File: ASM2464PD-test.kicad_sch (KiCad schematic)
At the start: 1 part

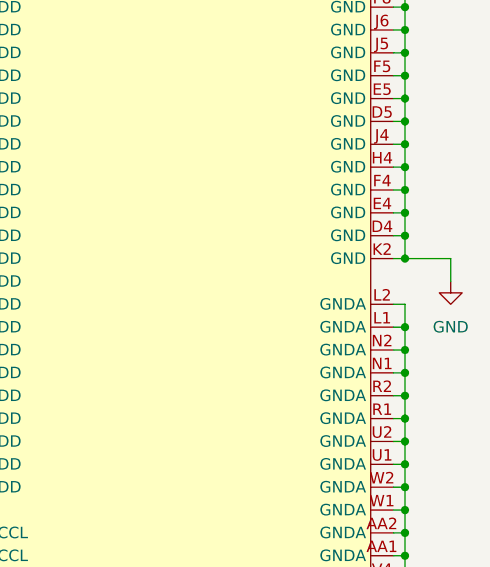
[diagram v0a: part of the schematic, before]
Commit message: Connected the 2 grounds
what's the difference anyway
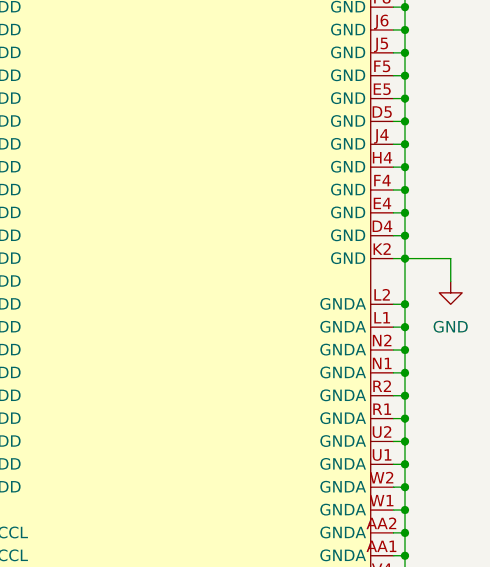
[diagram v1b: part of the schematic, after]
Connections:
- net GNDA is gone; now on net GND: U1.AA1 (GNDA), U1.AA12 (GNDA), U1.AA14 (GNDA), U1.AA16 (GNDA), U1.AA18 (GNDA), U1.AA2 (GNDA), U1.AA20 (GNDA), U1.AA21 (GNDA), U1.AA5 (GNDA), U1.AA9 (GNDA), U1.L1 (GNDA), U1.L2 (GNDA), U1.L4 (GNDA), U1.L5 (GNDA), U1.M20 (GNDA), U1.M21 (GNDA), U1.N1 (GNDA), U1.N17 (GNDA), U1.N18 (GNDA), U1.N2 (GNDA), U1.N4 (GNDA), U1.N5 (GNDA), U1.P17 (GNDA), U1.P18 (GNDA), U1.P20 (GNDA), U1.P21 (GNDA), U1.P4 (GNDA), U1.P5 (GNDA), U1.R1 (GNDA), U1.R2 (GNDA), U1.T17 (GNDA), U1.T18 (GNDA), U1.T20 (GNDA), U1.T21 (GNDA), U1.T4 (GNDA), U1.T5 (GNDA), U1.U1 (GNDA), U1.U17 (GNDA), U1.U18 (GNDA), U1.U2 (GNDA), U1.U4 (GNDA), U1.U5 (GNDA), U1.V11 (GNDA), U1.V13 (GNDA), U1.V14 (GNDA), U1.V16 (GNDA), U1.V17 (GNDA), U1.V18 (GNDA), U1.V20 (GNDA), U1.V21 (GNDA), U1.V4 (GNDA), U1.V5 (GNDA), U1.V6 (GNDA), U1.V8 (GNDA), U1.V9 (GNDA), U1.W1 (GNDA), U1.W2 (GNDA), U1.Y12 (GNDA), U1.Y14 (GNDA), U1.Y16 (GNDA), U1.Y18 (GNDA), U1.Y20 (GNDA), U1.Y21 (GNDA), U1.Y3 (GNDA), U1.Y5 (GNDA), U1.Y9 (GNDA)
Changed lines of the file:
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@@
   (junction (at 270.51 185.42) (diameter 0) (color 0 0 0 0)
   )
+  (junction (at 270.51 114.3) (diameter 0) (color 0 0 0 0)
+  )
   (junction (at 220.98 119.38) (diameter 0) (color 0 0 0 0)
   )
@@
     (stroke (width 0) (type default))
   )
+  (wire (pts (xy 270.51 109.22) (xy 270.51 114.3))
+    (stroke (width 0) (type default))
+  )

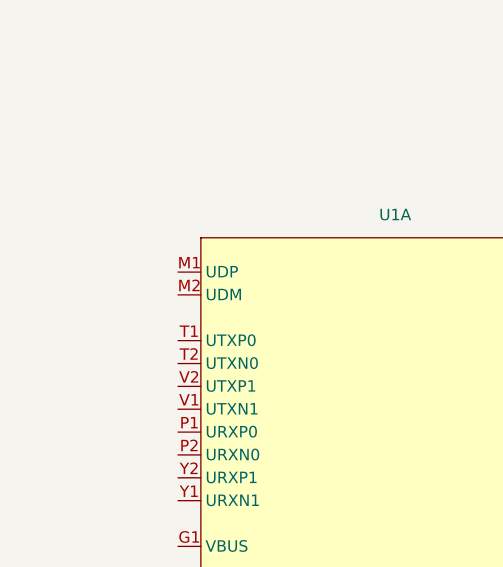
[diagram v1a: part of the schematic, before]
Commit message: Added some keywords to readme
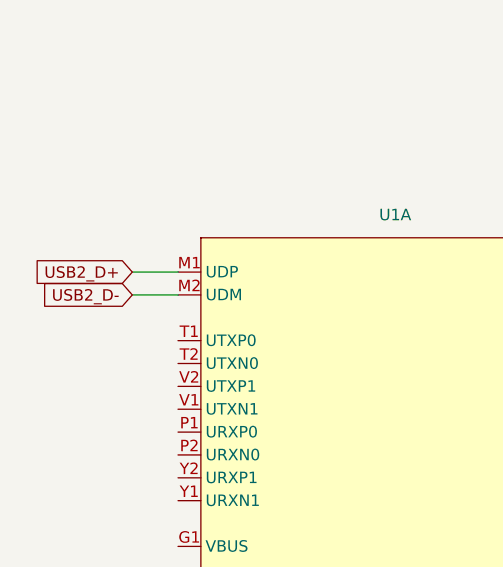
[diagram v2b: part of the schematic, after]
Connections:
- net USB2_D+: now reaches U1.M1 (UDP)
- net USB2_D-: now reaches U1.M2 (UDM)
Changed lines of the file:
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@@
+    (stroke (width 0) (type default))
+  )
+  (wire (pts (xy 59.69 93.98) (xy 64.77 93.98))
     (stroke (width 0) (type default))
   )
@@
     (stroke (width 0) (type default))
   )
+  (wire (pts (xy 59.69 96.52) (xy 64.77 96.52))
+    (stroke (width 0) (type default))
+  )
   (wire (pts (xy 269.24 213.36) (xy 270.51 213.36))
     (stroke (width 0) (type default))
@@
   (wire (pts (xy 269.24 223.52) (xy 270.51 223.52))
     (stroke (width 0) (type default))
+  )
+  (global_label "USB2_D-" (shape input) (at 59.69 96.52 180) (fields_autoplaced)
+    (effects (font (size 1.27 1.27)) (justify right))
+    (property "Intersheetrefs" "${INTERSHEET_REFS}" (at 47.8753 96.52 0)
+      (effects (font (size 1.27 1.27)) (justify right) hide)
+    )
+  )
+  (global_label "USB2_D+" (shape input) (at 59.69 93.98 180) (fields_autoplaced)
+    (effects (font (size 1.27 1.27)) (justify right))
+    (property "Intersheetrefs" "${INTERSHEET_REFS}" (at 47.8753 93.98 0)
+      (effects (font (size 1.27 1.27)) (justify right) hide)
+    )
   )
   (symbol (lib_id "power:GND") (at 275.59 111.76 0) (unit 1)
@@
   )
   (symbol (lib_id "A_my_stuff:ASM2464PD") (at 87.63 195.58 0) (unit 1)
-    (in_bom yes) (on_board yes) (dnp no) (fields_autoplaced)
+    (in_bom yes) (on_board yes) (dnp no)
     (property "Reference" "U1" (at 88.9 87.63 0)
       (effects (font (size 1.27 1.27)))

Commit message: Added ports and definitely didn't clone reddit board lol
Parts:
- added C1, C10, C11, C12, C13, C14, C15, C16, C2, C3, C4, C5, C6, C7, C8, C9: 0.22u, Capacitor_SMD:C_0402_1005Metric, symbol Device:C_Small
- added J1: USB_C_Receptacle, Connector_USB:USB_C_Receptacle_Amphenol_12401610E4-2A, symbol Connector:USB_C_Receptacle
- added J2: Bus_M.2_Socket_M, A_my_stuff:m-key, symbol Connector:Bus_M.2_Socket_M
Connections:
- net GND: now also J1.A1 (GND), J1.A12 (GND), J1.B1 (GND), J1.B12 (GND), J1.S1 (SHIELD), J2.1 (GND), J2.15 (GND), J2.21 (GND), J2.27 (GND), J2.3 (GND), J2.33 (GND), J2.39 (GND), J2.45 (GND), J2.51 (GND), J2.57 (GND), J2.71 (GND), J2.73 (GND), J2.75 (GND), J2.9 (GND)
- net USB2_D+: now also J1.A6 (D+), J1.B6 (D+)
- net USB2_D-: now also J1.A7 (D-), J1.B7 (D-)
- net PCIe_RX3+: now reaches U1.AA13 (PRXP3)
- net PCIe_RX3+: now also J2.7 (PERp3)
- net PCIe_TX3-: now reaches U1.AA15 (PTXN3)
- net PCIe_TX3-: now also C8.1
- net PCIe_TX2-: now reaches U1.AA17 (PTXN2)
- net PCIe_TX2-: now also C6.1
- net PCIe_RX2-: now reaches U1.AA19 (PRXN2)
- net PCIe_RX2-: now also J2.17 (PERn2)
- net CC1: now reaches U1.AA6 (CC1)
- net CC1: now also J1.A5 (CC1)
- net REFCLK+: now reaches U1.AA8 (REFCLKP0)
- net REFCLK+: now also J2.55 (REFCLKp)
- net PERST#: now reaches U1.G21 (PERST0#)
- net PERST#: now also J2.50 (~{PERST})
- net SBU2: now reaches U1.J1 (SBU2)
- net SBU2: now also J1.B8 (SBU2)
- net SBU1: now reaches U1.K1 (SBU1)
- net SBU1: now also J1.A8 (SBU1)
- net PCIe_RX0-: now reaches U1.N20 (PRXN0)
- net PCIe_RX0-: now also J2.41 (PERn0/SATA-B+)
- net PCIe_RX0+: now reaches U1.N21 (PRXP0)
- net PCIe_RX0+: now also J2.43 (PERp0/SATA-B-)
- net URX0+: now reaches U1.P1 (URXP0)
- net URX0+: now also C10.2
- net URX0-: now reaches U1.P2 (URXN0)
- net URX0-: now also C9.2
- net PCIe_TX0+: now reaches U1.R20 (PTXP0)
- net PCIe_TX0+: now also C1.1
- net PCIe_TX0-: now reaches U1.R21 (PTXN0)
- net PCIe_TX0-: now also C2.1
- net UTX0+: now reaches U1.T1 (UTXP0)
- net UTX0+: now also C12.2
- net UTX0-: now reaches U1.T2 (UTXN0)
- net UTX0-: now also C11.2
- net PCIe_TX1+: now reaches U1.U20 (PTXP1)
- net PCIe_TX1+: now also C3.1
- net PCIe_TX1-: now reaches U1.U21 (PTXN1)
- net PCIe_TX1-: now also C4.1
- net UTX1-: now reaches U1.V1 (UTXN1)
- net UTX1-: now also C15.2
- net UTX1+: now reaches U1.V2 (UTXP1)
- net UTX1+: now also C16.2
- net PCIe_RX1-: now reaches U1.W20 (PRXN1)
- net PCIe_RX1-: now also J2.29 (PERn1)
- net PCIe_RX1+: now reaches U1.W21 (PRXP1)
- net PCIe_RX1+: now also J2.31 (PERp1)
- net URX1-: now reaches U1.Y1 (URXN1)
- net URX1-: now also C13.2
- net PCIe_RX3-: now reaches U1.Y13 (PRXN3)
- net PCIe_RX3-: now also J2.5 (PERn3)
- net PCIe_TX3+: now reaches U1.Y15 (PTXP3)
- net PCIe_TX3+: now also C7.1
- net PCIe_TX2+: now reaches U1.Y17 (PTXP2)
- net PCIe_TX2+: now also C5.1
- net PCIe_RX2+: now reaches U1.Y19 (PRXP2)
- net PCIe_RX2+: now also J2.19 (PERp2)
- net URX1+: now reaches U1.Y2 (URXP1)
- net URX1+: now also C14.2
- net CC2: now reaches U1.Y6 (CC2)
- net CC2: now also J1.B5 (CC2)
- net REFCLK-: now reaches U1.Y8 (REFCLKN0)
- net REFCLK-: now also J2.53 (REFCLKn)
- new net: J1.A4 (VBUS), J1.A9 (VBUS), J1.B4 (VBUS), J1.B9 (VBUS)
- new net: J2.12 (3.3V), J2.14 (3.3V), J2.16 (3.3V), J2.18 (3.3V), J2.2 (3.3V), J2.4 (3.3V), J2.70 (3.3V), J2.72 (3.3V), J2.74 (3.3V)
- new net PCIe_TX0_C+: C1.2, J2.49 (PETp0/SATA-A+)
- new net PCIe_TX0_C-: C2.2, J2.47 (PETn0/SATA-A-)
- new net PCIe_TX1_C+: C3.2, J2.37 (PETp1)
- new net PCIe_TX1_C-: C4.2, J2.35 (PETn1)
- new net PCIe_TX2_C+: C5.2, J2.25 (PETp2)
- new net PCIe_TX2_C-: C6.2, J2.23 (PETn2)
- new net PCIe_TX3_C+: C7.2, J2.13 (PETp3)
- new net PCIe_TX3_C-: C8.2, J2.11 (PETn3)
- new net URX0_C+: C10.1, J1.B11 (RX1+)
- new net URX0_C-: C9.1, J1.B10 (RX1-)
- new net URX1_C+: C14.1, J1.A11 (RX2+)
- new net URX1_C-: C13.1, J1.A10 (RX2-)
- new net UTX0_C+: C12.1, J1.A2 (TX1+)
- new net UTX0_C-: C11.1, J1.A3 (TX1-)
- new net UTX1_C+: C16.1, J1.B2 (TX2+)
- new net UTX1_C-: C15.1, J1.B3 (TX2-)
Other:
- note added: "idk if these caps are the right value. these signals probably need some more protection and stuff on them too."
- moved on the sheet: U1A, U1B, U1C

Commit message: Tried adding power fills under the chip
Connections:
- net VCCH: now reaches U1.D13 (VCCH), U1.D6 (VCCH), U1.D8 (VCCH), U1.D9 (VCCH), U1.E13 (VCCH), U1.E6 (VCCH), U1.E8 (VCCH), U1.E9 (VCCH), U1.F13 (VCCH), U1.F6 (VCCH), U1.H6 (VCCH)
- net VDD: now reaches U1.D14 (VDD), U1.D16 (VDD), U1.E11 (VDD), U1.E14 (VDD), U1.E16 (VDD), U1.F11 (VDD), U1.F14 (VDD), U1.F16 (VDD), U1.F9 (VDD), U1.H11 (VDD), U1.H13 (VDD), U1.H14 (VDD), U1.H16 (VDD), U1.H9 (VDD), U1.J13 (VDD), U1.J14 (VDD), U1.J16 (VDD), U1.J17 (VDD), U1.J18 (VDD), U1.J20 (VDD), U1.J21 (VDD), U1.J8 (VDD), U1.J9 (VDD), U1.K20 (VDD), U1.K21 (VDD), U1.L11 (VDD), U1.L14 (VDD), U1.L8 (VDD), U1.N14 (VDD), U1.N8 (VDD), U1.P13 (VDD), U1.P14 (VDD), U1.P8 (VDD), U1.T11 (VDD), U1.T13 (VDD), U1.T14 (VDD), U1.T8 (VDD), U1.T9 (VDD), U1.U8 (VDD), U1.U9 (VDD)
- net VCCL: now reaches U1.L16 (VCCL), U1.L17 (VCCL), U1.L18 (VCCL), U1.L20 (VCCL), U1.L21 (VCCL), U1.L6 (VCCL), U1.N16 (VCCL), U1.N6 (VCCL), U1.P16 (VCCL), U1.P6 (VCCL), U1.T16 (VCCL), U1.T6 (VCCL), U1.U11 (VCCL), U1.U13 (VCCL), U1.U14 (VCCL), U1.U16 (VCCL), U1.U6 (VCCL)
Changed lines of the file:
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@@
   (junction (at 398.78 228.6) (diameter 0) (color 0 0 0 0)
   )
+  (junction (at 349.25 20.32) (diameter 0) (color 0 0 0 0)
+  )
   (junction (at 349.25 76.2) (diameter 0) (color 0 0 0 0)
   )
@@
   (junction (at 349.25 137.16) (diameter 0) (color 0 0 0 0)
   )
+  (junction (at 349.25 124.46) (diameter 0) (color 0 0 0 0)
+  )
   (junction (at 398.78 152.4) (diameter 0) (color 0 0 0 0)
   )
@@
   (junction (at 349.25 134.62) (diameter 0) (color 0 0 0 0)
   )
+  (junction (at 349.25 170.18) (diameter 0) (color 0 0 0 0)
+  )
   (junction (at 398.78 111.76) (diameter 0) (color 0 0 0 0)
   )
@@
     (stroke (width 0) (type default))
   )
+  (wire (pts (xy 345.44 19.05) (xy 345.44 20.32))
+    (stroke (width 0) (type default))
+  )
   (wire (pts (xy 397.51 220.98) (xy 398.78 220.98))
     (stroke (width 0) (type default))
@@
     (stroke (width 0) (type default))
   )
+  (wire (pts (xy 346.71 170.18) (xy 349.25 170.18))
+    (stroke (width 0) (type default))
+  )
   (wire (pts (xy 397.51 180.34) (xy 398.78 180.34))
     (stroke (width 0) (type default))
@@
     (stroke (width 0) (type default))
   )
+  (wire (pts (xy 346.71 124.46) (xy 349.25 124.46))
+    (stroke (width 0) (type default))
+  )
   (wire (pts (xy 349.25 175.26) (xy 349.25 177.8))
     (stroke (width 0) (type default))
@@
   )
   (wire (pts (xy 55.88 119.38) (xy 63.5 119.38))
+    (stroke (width 0) (type default))
+  )
+  (wire (pts (xy 345.44 20.32) (xy 349.25 20.32))
     (stroke (width 0) (type default))
   )
@@
     )
   )
+  (global_label "VCCH" (shape input) (at 346.71 170.18 180) (fields_autoplaced)
+    (effects (font (size 1.27 1.27)) (justify right))
+    (property "Intersheetrefs" "${INTERSHEET_REFS}" (at 338.7657 170.18 0)
+      (effects (font (size 1.27 1.27)) (justify right) hide)
+    )
+  )
   (global_label "PCIe_TX0+" (shape input) (at 265.43 128.27 180) (fields_autoplaced)
     (effects (font (size 1.27 1.27)) (justify right))
@@
     (effects (font (size 1.27 1.27)) (justify right))
     (property "Intersheetrefs" "${INTERSHEET_REFS}" (at 253.7967 115.57 0)
+      (effects (font (size 1.27 1.27)) (justify right) hide)
+    )
+  )
+  (global_label "VCCL" (shape input) (at 346.71 124.46 180) (fields_autoplaced)
+    (effects (font (size 1.27 1.27)) (justify right))
+    (property "Intersheetrefs" "${INTERSHEET_REFS}" (at 339.0681 124.46 0)
       (effects (font (size 1.27 1.27)) (justify right) hide)
     )
@@
         )
       )
+    )
+  )
+  (symbol (lib_id "power:VDD") (at 345.44 19.05 0) (unit 1)
+    (in_bom yes) (on_board yes) (dnp no) (fields_autoplaced)
+    (property "Reference" "#PWR05" (at 345.44 22.86 0)
+      (effects (font (size 1.27 1.27)) hide)
+    )
+    (property "Value" "VDD" (at 345.44 13.97 0)
+      (effects (font (size 1.27 1.27)))
+    )
+    (property "Footprint" "" (at 345.44 19.05 0)
+      (effects (font (size 1.27 1.27)) hide)
+    )
+    (property "Datasheet" "" (at 345.44 19.05 0)
+      (effects (font (size 1.27 1.27)) hide)
+    )
+    (pin "1")
+    (instances
+      (project "ASM2464PD-test"
+        (path "/b2a945ac-f788-482b-9831-47d865c602eb"
+          (reference "#PWR05") (unit 1)
+        )
+      )

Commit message: forgor some power pins
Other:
- company: (none) -> WifiCable
- title: (none) -> ASM2464PD-test
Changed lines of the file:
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@@
 (kicad_sch (version 20230121) (generator eeschema)
   (paper "A3")
+  (title_block
+    (title "ASM2464PD-test")
+    (company "WifiCable")
+  )
   (junction (at 398.78 114.3) (diameter 0) (color 0 0 0 0)
   )

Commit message: Labeled power rails, upgraded to KiCad 8
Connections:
- net 3.3VA: now reaches U1.H5 (VCCA33)
- net VCCH renamed 3.3V
- net VCCL renamed 1.8V
- net VDD renamed 1.05V

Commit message: Updated symbol to match reference schematic
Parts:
- added unit 4 of U1
- added unit 5 of U1
- added unit 6 of U1
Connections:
- net 1.8V: now also U1.L16 (VCCL), U1.L17 (VCCL), U1.L18 (VCCL), U1.L20 (VCCL), U1.L21 (VCCL), U1.L6 (VCCL), U1.N16 (VCCL), U1.N6 (VCCL), U1.P16 (VCCL), U1.P6 (VCCL), U1.T16 (VCCL), U1.T6 (VCCL), U1.U11 (VCCL), U1.U13 (VCCL), U1.U14 (VCCL), U1.U16 (VCCL), U1.U6 (VCCL); no longer U1.L16 (VCCL), U1.L17 (VCCL), U1.L18 (VCCL), U1.L20 (VCCL), U1.L21 (VCCL), U1.L6 (VCCL), U1.N16 (VCCL), U1.N6 (VCCL), U1.P16 (VCCL), U1.P6 (VCCL), U1.T16 (VCCL), U1.T6 (VCCL), U1.U11 (VCCL), U1.U13 (VCCL), U1.U14 (VCCL), U1.U16 (VCCL), U1.U6 (VCCL)
- net 3.3V: now also U1.D13 (VCCH), U1.D6 (VCCH), U1.D8 (VCCH), U1.D9 (VCCH), U1.E13 (VCCH), U1.E6 (VCCH), U1.E8 (VCCH), U1.E9 (VCCH), U1.F13 (VCCH), U1.F6 (VCCH), U1.H6 (VCCH); no longer U1.D13 (VCCH), U1.D6 (VCCH), U1.D8 (VCCH), U1.D9 (VCCH), U1.E13 (VCCH), U1.E6 (VCCH), U1.E8 (VCCH), U1.E9 (VCCH), U1.F13 (VCCH), U1.F6 (VCCH), U1.H6 (VCCH)
- net 3.3VA: now also U1.H5 (VCCA33); no longer U1.H5 (VCCA33)
- net GND: now also U1.AA1 (GNDA), U1.AA12 (GNDA), U1.AA14 (GNDA), U1.AA16 (GNDA), U1.AA18 (GNDA), U1.AA2 (GNDA), U1.AA20 (GNDA), U1.AA21 (GNDA), U1.AA5 (GNDA), U1.AA9 (GNDA), U1.L1 (GNDA), U1.L2 (GNDA), U1.L4 (GNDA), U1.L5 (GNDA), U1.M20 (GNDA), U1.M21 (GNDA), U1.N1 (GNDA), U1.N17 (GNDA), U1.N18 (GNDA), U1.N2 (GNDA), U1.N4 (GNDA), U1.N5 (GNDA), U1.P17 (GNDA), U1.P18 (GNDA), U1.P20 (GNDA), U1.P21 (GNDA), U1.P4 (GNDA), U1.P5 (GNDA), U1.R1 (GNDA), U1.R2 (GNDA), U1.T17 (GNDA), U1.T18 (GNDA), U1.T20 (GNDA), U1.T21 (GNDA), U1.T4 (GNDA), U1.T5 (GNDA), U1.U1 (GNDA), U1.U17 (GNDA), U1.U18 (GNDA), U1.U2 (GNDA), U1.U4 (GNDA), U1.U5 (GNDA), U1.V11 (GNDA), U1.V13 (GNDA), U1.V14 (GNDA), U1.V16 (GNDA), U1.V17 (GNDA), U1.V18 (GNDA), U1.V20 (GNDA), U1.V21 (GNDA), U1.V4 (GNDA), U1.V5 (GNDA), U1.V6 (GNDA), U1.V8 (GNDA), U1.V9 (GNDA), U1.W1 (GNDA), U1.W2 (GNDA), U1.Y12 (GNDA), U1.Y14 (GNDA), U1.Y16 (GNDA), U1.Y18 (GNDA), U1.Y20 (GNDA), U1.Y21 (GNDA), U1.Y3 (GNDA), U1.Y5 (GNDA), U1.Y9 (GNDA); no longer U1.AA1 (GNDA), U1.AA12 (GNDA), U1.AA14 (GNDA), U1.AA16 (GNDA), U1.AA18 (GNDA), U1.AA2 (GNDA), U1.AA20 (GNDA), U1.AA21 (GNDA), U1.AA5 (GNDA), U1.AA9 (GNDA), U1.L1 (GNDA), U1.L2 (GNDA), U1.L4 (GNDA), U1.L5 (GNDA), U1.M20 (GNDA), U1.M21 (GNDA), U1.N1 (GNDA), U1.N17 (GNDA), U1.N18 (GNDA), U1.N2 (GNDA), U1.N4 (GNDA), U1.N5 (GNDA), U1.P17 (GNDA), U1.P18 (GNDA), U1.P20 (GNDA), U1.P21 (GNDA), U1.P4 (GNDA), U1.P5 (GNDA), U1.R1 (GNDA), U1.R2 (GNDA), U1.T17 (GNDA), U1.T18 (GNDA), U1.T20 (GNDA), U1.T21 (GNDA), U1.T4 (GNDA), U1.T5 (GNDA), U1.U1 (GNDA), U1.U17 (GNDA), U1.U18 (GNDA), U1.U2 (GNDA), U1.U4 (GNDA), U1.U5 (GNDA), U1.V11 (GNDA), U1.V13 (GNDA), U1.V14 (GNDA), U1.V16 (GNDA), U1.V17 (GNDA), U1.V18 (GNDA), U1.V20 (GNDA), U1.V21 (GNDA), U1.V4 (GNDA), U1.V5 (GNDA), U1.V6 (GNDA), U1.V8 (GNDA), U1.V9 (GNDA), U1.W1 (GNDA), U1.W2 (GNDA), U1.Y12 (GNDA), U1.Y14 (GNDA), U1.Y16 (GNDA), U1.Y18 (GNDA), U1.Y20 (GNDA), U1.Y21 (GNDA), U1.Y3 (GNDA), U1.Y5 (GNDA), U1.Y9 (GNDA)
- net PERST#: no longer U1.G21 (PERST0#)
- removed net 1.05V: U1.D14 (VDD), U1.D16 (VDD), U1.E11 (VDD), U1.E14 (VDD), U1.E16 (VDD), U1.F11 (VDD), U1.F14 (VDD), U1.F16 (VDD), U1.F9 (VDD), U1.H11 (VDD), U1.H13 (VDD), U1.H14 (VDD), U1.H16 (VDD), U1.H9 (VDD), U1.J13 (VDD), U1.J14 (VDD), U1.J16 (VDD), U1.J17 (VDD), U1.J18 (VDD), U1.J20 (VDD), U1.J21 (VDD), U1.J8 (VDD), U1.J9 (VDD), U1.K20 (VDD), U1.K21 (VDD), U1.L11 (VDD), U1.L14 (VDD), U1.L8 (VDD), U1.N14 (VDD), U1.N8 (VDD), U1.P13 (VDD), U1.P14 (VDD), U1.P8 (VDD), U1.T11 (VDD), U1.T13 (VDD), U1.T14 (VDD), U1.T8 (VDD), U1.T9 (VDD), U1.U8 (VDD), U1.U9 (VDD)
- new net 0.95V: U1.D14 (VDD), U1.D16 (VDD), U1.E11 (VDD), U1.E14 (VDD), U1.E16 (VDD), U1.F11 (VDD), U1.F14 (VDD), U1.F16 (VDD), U1.F9 (VDD), U1.H11 (VDD), U1.H13 (VDD), U1.H14 (VDD), U1.H16 (VDD), U1.H9 (VDD), U1.J13 (VDD), U1.J14 (VDD), U1.J16 (VDD), U1.J17 (VDD), U1.J18 (VDD), U1.J20 (VDD), U1.J21 (VDD), U1.J8 (VDD), U1.J9 (VDD), U1.K20 (VDD), U1.K21 (VDD), U1.L11 (VDD), U1.L14 (VDD), U1.L8 (VDD), U1.N14 (VDD), U1.N8 (VDD), U1.P13 (VDD), U1.P14 (VDD), U1.P8 (VDD), U1.T11 (VDD), U1.T13 (VDD), U1.T14 (VDD), U1.T8 (VDD), U1.T9 (VDD), U1.U8 (VDD), U1.U9 (VDD)
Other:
- moved on the sheet: C1, C10, C11, C12, C13, C14, C15, C16, C2, C3, C4, C5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
